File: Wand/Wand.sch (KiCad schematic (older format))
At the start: 20 parts, among them IC1 ATMEGA328P-A, J1 TIP, P1 ISP, P2 BASE, U1 OPA336U, U2 MPU-6050, Y1 16MHz

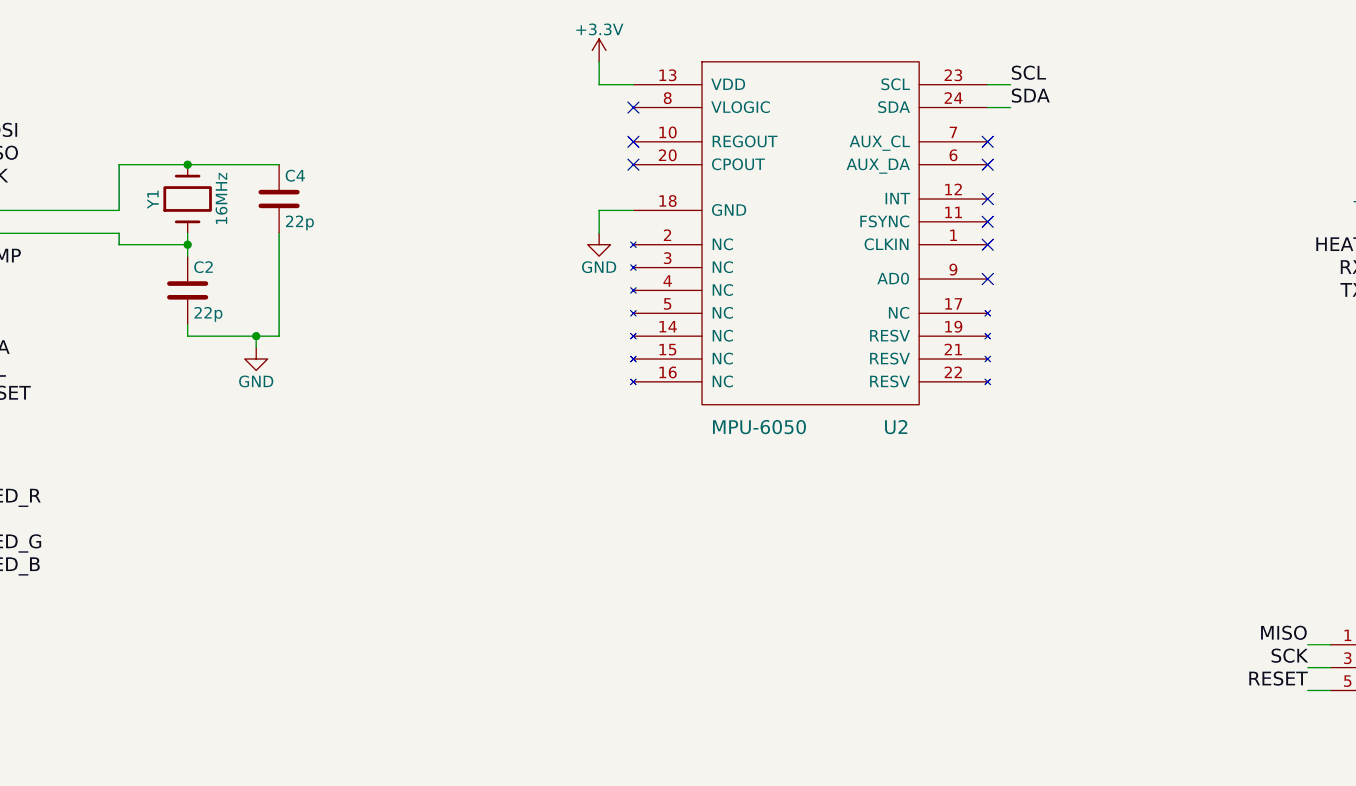
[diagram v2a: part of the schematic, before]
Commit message: Added the support passive components for the MPU-6050.
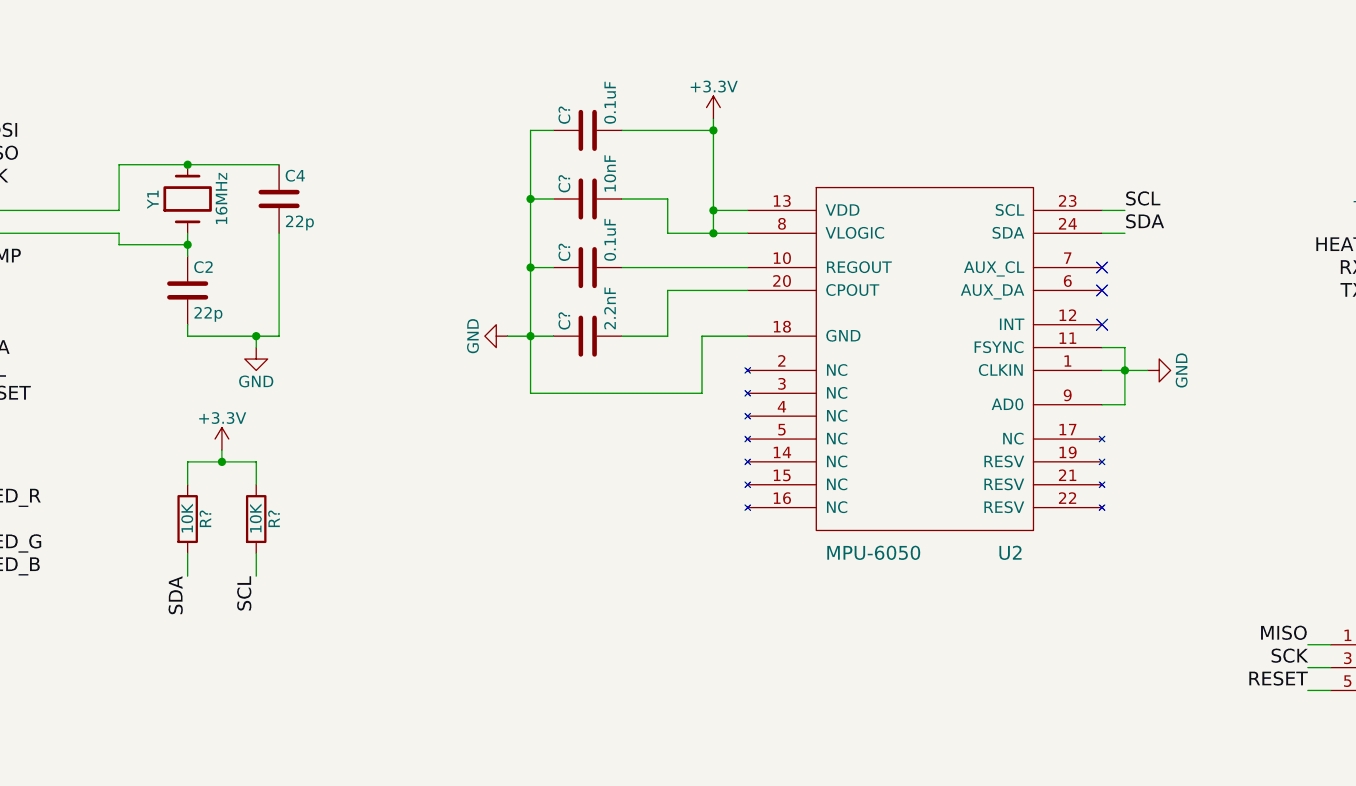
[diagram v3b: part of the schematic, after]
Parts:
- added C?: 2.2nF, symbol C
- added C? (x2): 0.1uF, symbol C
- added C?: 10nF, symbol C
- added R? (x2): 10K, symbol R
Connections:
- net +3V3: now also U2.8 (VLOGIC), C?.2, C?.2, R?.1, R?.1
- net GND: now also U2.1 (CLKIN), U2.11 (FSYNC), U2.9 (AD0), C?.1, C?.1, C?.1, C?.1
- net SCL: now also R?.2
- net SDA: now also R?.2
- net at U2.10 (REGOUT): now also C?.2
- net at U2.20 (CPOUT): now also C?.2
- no-connect marks 23 -> 17
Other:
- moved on the sheet: U2
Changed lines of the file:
@@
 L MPU-6050 U2
 U 1 1 56411594
-P 7450 2100
-F 0 "U2" H 7800 1400 60  0000 C CNN
-F 1 "MPU-6050" H 7200 1400 60  0000 C CNN
-F 2 "" H 7450 1850 60  0000 C CNN
-F 3 "" H 7450 1850 60  0000 C CNN
-	1    7450 2100
+P 7950 2650
+F 0 "U2" H 8300 1950 60  0000 C CNN
+F 1 "MPU-6050" H 7700 1950 60  0000 C CNN
+F 2 "" H 7950 2400 60  0000 C CNN
+F 3 "" H 7950 2400 60  0000 C CNN
+	1    7950 2650
 	1    0    0    -1
 $EndComp
@@
 Wire Wire Line
 	9900 2350 10000 2350
-Text Label 8300 1400 0    60   ~ 0
+Text Label 8800 1950 0    60   ~ 0
 SDA
-Text Label 8300 1300 0    60   ~ 0
+Text Label 8800 1850 0    60   ~ 0
 SCL
 Wire Wire Line
-	8300 1300 8200 1300
-Wire Wire Line
-	8200 1400 8300 1400
-$Comp
-L GND #PWR016
-U 1 1 56419575
-P 6500 1950
-F 0 "#PWR016" H 6500 1700 50  0001 C CNN
-F 1 "GND" H 6500 1800 50  0000 C CNN
-F 2 "" H 6500 1950 60  0000 C CNN
-F 3 "" H 6500 1950 60  0000 C CNN
-	1    6500 1950
-	1    0    0    -1
-$EndComp
-Wire Wire Line
-	6500 1850 6500 1950
-Wire Wire Line
-	6500 1850 6650 1850
-Wire Wire Line
-	6650 1300 6500 1300
-Wire Wire Line
-	6500 1300 6500 1200
+	8800 1850 8700 1850
+Wire Wire Line
+	8700 1950 8800 1950
+Wire Wire Line
+	7000 1850 7150 1850
+Wire Wire Line
+	7000 1450 7000 1950
 Text Label 3750 2500 0    60   ~ 0
 SDA
@@
 NoConn ~ 3600 1350
 NoConn ~ 3600 1250
-NoConn ~ 6650 1400
-NoConn ~ 6650 1550
-NoConn ~ 6650 1650
-NoConn ~ 8200 2150
-NoConn ~ 8200 2000
-NoConn ~ 8200 1900
-NoConn ~ 8200 1800
-NoConn ~ 8200 1650
-NoConn ~ 8200 1550
+NoConn ~ 8700 2350
+NoConn ~ 8700 2200
+NoConn ~ 8700 2100
 $Comp
 L PWR_FLAG #FLG017
@@
 L +3.3V #PWR?
 U 1 1 5647B486
-P 6500 1200
-F 0 "#PWR?" H 6500 1050 50  0001 C CNN
-F 1 "+3.3V" H 6500 1340 50  0000 C CNN
-F 2 "" H 6500 1200 60  0000 C CNN
-F 3 "" H 6500 1200 60  0000 C CNN
-	1    6500 1200
+P 7000 1450
+F 0 "#PWR?" H 7000 1300 50  0001 C CNN
+F 1 "+3.3V" H 7000 1590 50  0000 C CNN
+F 2 "" H 7000 1450 60  0000 C CNN
+F 3 "" H 7000 1450 60  0000 C CNN
+	1    7000 1450
 	1    0    0    -1
 $EndComp
@@
 Text Label 9850 2150 2    60   ~ 0
 RX
+$Comp
+L C C?
+U 1 1 5647F0EB
+P 6450 2400
+F 0 "C?" H 6475 2500 50  0000 L CNN
+F 1 "2.2nF" H 6475 2300 50  0000 L CNN
+F 2 "" H 6488 2250 30  0000 C CNN
+F 3 "" H 6450 2400 60  0000 C CNN
+	1    6450 2400
+	0    -1   -1   0
+$EndComp
+$Comp
+L GND #PWR?
+U 1 1 5647F13E
+P 6100 2400
+F 0 "#PWR?" H 6100 2150 50  0001 C CNN
+F 1 "GND" H 6100 2250 50  0000 C CNN
+F 2 "" H 6100 2400 60  0000 C CNN
+F 3 "" H 6100 2400 60  0000 C CNN
+	1    6100 2400
+	0    1    1    0
+$EndComp
+$Comp
+L GND #PWR?
+U 1 1 5647F1D7
+P 8900 2550
+F 0 "#PWR?" H 8900 2300 50  0001 C CNN
+F 1 "GND" H 8900 2400 50  0000 C CNN
+F 2 "" H 8900 2550 60  0000 C CNN
+F 3 "" H 8900 2550 60  0000 C CNN
+	1    8900 2550
+	0    -1   -1   0
+$EndComp
+Wire Wire Line
+	8800 2700 8700 2700
+$Comp
+L C C?
+U 1 1 5647F6E8
+P 6450 2100
+F 0 "C?" H 6475 2200 50  0000 L CNN
+F 1 "0.1uF" H 6475 2000 50  0000 L CNN
+F 2 "" H 6488 1950 30  0000 C CNN
+F 3 "" H 6450 2100 60  0000 C CNN
+	1    6450 2100
+	0    -1   -1   0
+$EndComp
+Wire Wire Line
+	6800 2200 7150 2200
+Wire Wire Line
+	6600 2400 6800 2400
+Wire Wire Line
+	6600 2100 7150 2100
+Wire Wire Line
+	6300 2100 6200 2100
+Wire Wire Line
+	6200 1500 6200 2650
+Wire Wire Line
+	6100 2400 6300 2400
+Connection ~ 6200 2400
+$Comp
+L C C?
+U 1 1 5647FB65
+P 6450 1800
+F 0 "C?" H 6475 1900 50  0000 L CNN
+F 1 "10nF" H 6475 1700 50  0000 L CNN
+F 2 "" H 6488 1650 30  0000 C CNN
+F 3 "" H 6450 1800 60  0000 C CNN
+	1    6450 1800
+	0    -1   -1   0
+$EndComp
+Wire Wire Line
+	6300 1800 6200 1800
+Connection ~ 6200 2100
+Wire Wire Line
+	7150 1950 6800 1950
+Wire Wire Line
+	6800 1950 6800 1800
+Wire Wire Line
+	6800 1800 6600 1800
+Wire Wire Line
+	6800 2400 6800 2200
+Wire Wire Line
+	7150 2400 6950 2400
+Wire Wire Line
+	6950 2400 6950 2650
+Wire Wire Line
+	6950 2650 6200 2650
+$Comp
+L C C?
+U 1 1 5647FEFB
+P 6450 1500
+F 0 "C?" H 6475 1600 50  0000 L CNN
+F 1 "0.1uF" H 6475 1400 50  0000 L CNN
+F 2 "" H 6488 1350 30  0000 C CNN
+F 3 "" H 6450 1500 60  0000 C CNN
+	1    6450 1500
+	0    -1   -1   0
+$EndComp
+Wire Wire Line
+	6600 1500 7000 1500
+Connection ~ 7000 1500
+Wire Wire Line
+	6300 1500 6200 1500
+Connection ~ 6200 1800
+Connection ~ 7000 1950
+Connection ~ 7000 1850
+Wire Wire Line
+	8700 2450 8800 2450
+Wire Wire Line
+	8800 2450 8800 2700
+Wire Wire Line
+	8700 2550 8900 2550
+Connection ~ 8800 2550
+$Comp
+L R R?
+U 1 1 56481F9A
+P 4700 3200
+F 0 "R?" V 4780 3200 50  0000 C CNN
+F 1 "10K" V 4700 3200 50  0000 C CNN
+F 2 "" V 4630 3200 30  0000 C CNN
+F 3 "" H 4700 3200 30  0000 C CNN
+	1    4700 3200
+	1    0    0    -1
+$EndComp
+$Comp
+L R R?
+U 1 1 56481FFA
+P 5000 3200
+F 0 "R?" V 5080 3200 50  0000 C CNN
+F 1 "10K" V 5000 3200 50  0000 C CNN
+F 2 "" V 4930 3200 30  0000 C CNN
+F 3 "" H 5000 3200 30  0000 C CNN
+	1    5000 3200
+	1    0    0    -1
+$EndComp
+$Comp
+L +3.3V #PWR?
+U 1 1 56482043
+P 4850 2900
+F 0 "#PWR?" H 4850 2750 50  0001 C CNN
+F 1 "+3.3V" H 4850 3040 50  0000 C CNN
+F 2 "" H 4850 2900 60  0000 C CNN
+F 3 "" H 4850 2900 60  0000 C CNN
+	1    4850 2900
+	1    0    0    -1
+$EndComp
+Wire Wire Line
+	4700 3050 4700 2950
+Wire Wire Line
+	4700 2950 5000 2950
+Wire Wire Line
+	4850 2950 4850 2900
+Wire Wire Line
+	5000 2950 5000 3050
+Connection ~ 4850 2950
+Text Label 4700 3450 3    60   ~ 0
+SDA
+Text Label 5000 3450 3    60   ~ 0
+SCL
+Wire Wire Line
+	5000 3350 5000 3450
+Wire Wire Line
+	4700 3350 4700 3450
 $EndSCHEMATC

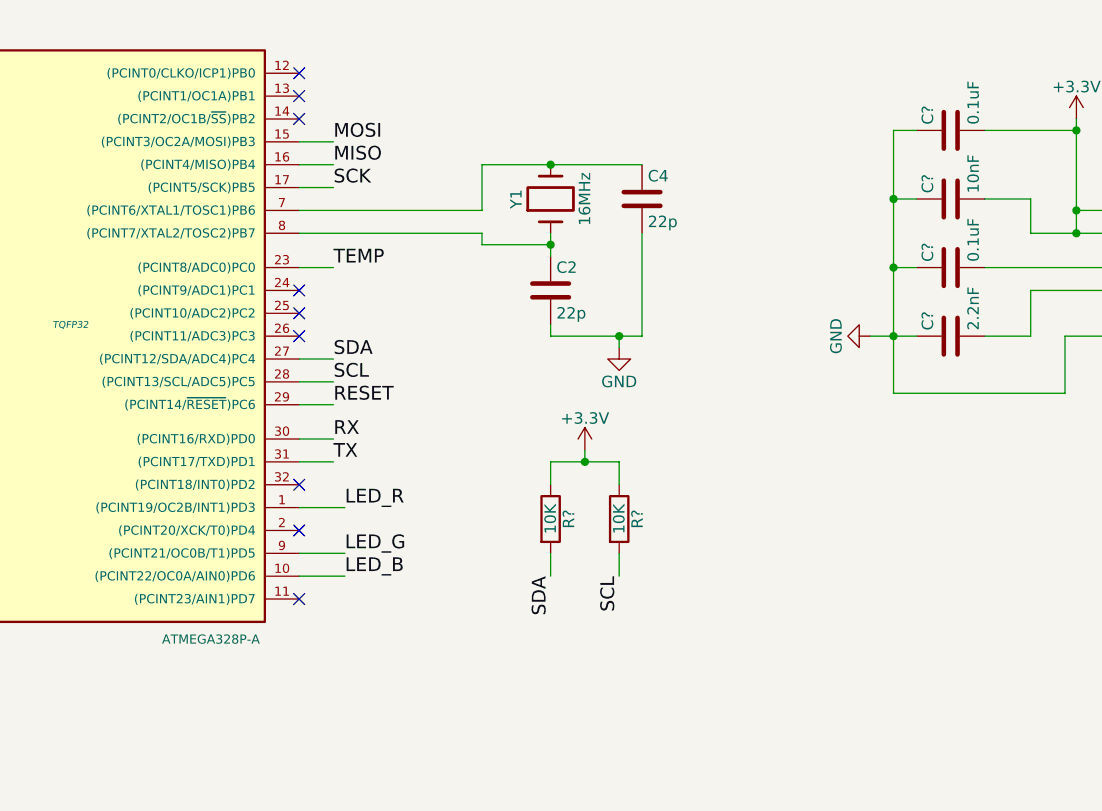
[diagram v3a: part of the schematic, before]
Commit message: Corrected the ATMega 328 part number, needed the 28-pin VQFN package 4x4mm
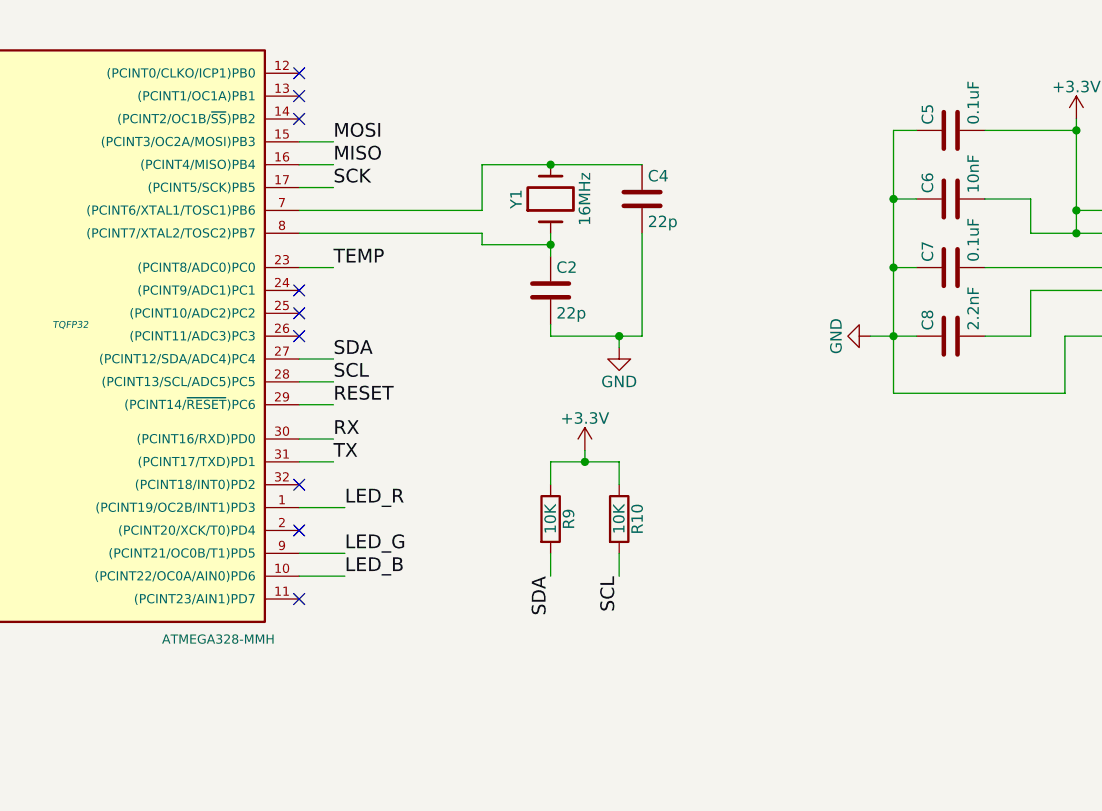
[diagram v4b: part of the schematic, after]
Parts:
- IC1: value ATMEGA328P-A -> ATMEGA328-MMH
- gave numbers to parts that had none: 6
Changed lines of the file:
@@
 P 2600 2350
 F 0 "IC1" H 1850 3600 40  0000 L BNN
-F 1 "ATMEGA328P-A" H 3000 950 40  0000 L BNN
+F 1 "ATMEGA328-MMH" H 3000 950 40  0000 L BNN
 F 2 "TQFP32" H 2600 2350 30  0000 C CIN
 F 3 "" H 2600 2350 60  0000 C CNN
@@
 $EndComp
 $Comp
-L GND #PWR02
+L GND #PWR6
 U 1 1 5641252D
 P 3700 6450
-F 0 "#PWR02" H 3700 6200 50  0001 C CNN
+F 0 "#PWR6" H 3700 6200 50  0001 C CNN
 F 1 "GND" H 3700 6300 50  0000 C CNN
 F 2 "" H 3700 6450 60  0000 C CNN
@@
 SENS
 $Comp
-L GND #PWR03
+L GND #PWR4
 U 1 1 56412884
 P 2650 6450
-F 0 "#PWR03" H 2650 6200 50  0001 C CNN
+F 0 "#PWR4" H 2650 6200 50  0001 C CNN
 F 1 "GND" H 2650 6300 50  0000 C CNN
 F 2 "" H 2650 6450 60  0000 C CNN
@@
 $EndComp
 $Comp
-L GND #PWR04
+L GND #PWR7
 U 1 1 564128BC
 P 4750 6450
-F 0 "#PWR04" H 4750 6200 50  0001 C CNN
+F 0 "#PWR7" H 4750 6200 50  0001 C CNN
 F 1 "GND" H 4750 6300 50  0000 C CNN
 F 2 "" H 4750 6450 60  0000 C CNN
@@
 TEMP
 $Comp
-L +5V #PWR05
+L +5V #PWR3
 U 1 1 564142EE
 P 2000 5050
-F 0 "#PWR05" H 2000 4900 50  0001 C CNN
+F 0 "#PWR3" H 2000 4900 50  0001 C CNN
 F 1 "+5V" H 2000 5190 50  0000 C CNN
 F 2 "" H 2000 5050 60  0000 C CNN
@@
 $EndComp
 $Comp
-L GND #PWR06
+L GND #PWR12
 U 1 1 5641471A
 P 7800 5050
-F 0 "#PWR06" H 7800 4800 50  0001 C CNN
+F 0 "#PWR12" H 7800 4800 50  0001 C CNN
 F 1 "GND" H 7800 4900 50  0000 C CNN
 F 2 "" H 7800 5050 60  0000 C CNN
@@
 TEMP
 $Comp
-L GND #PWR07
+L GND #PWR9
 U 1 1 56415081
 P 5000 2450
-F 0 "#PWR07" H 5000 2200 50  0001 C CNN
+F 0 "#PWR9" H 5000 2200 50  0001 C CNN
 F 1 "GND" H 5000 2300 50  0000 C CNN
 F 2 "" H 5000 2450 60  0000 C CNN
@@
 $EndComp
 $Comp
-L GND #PWR09
+L GND #PWR2
 U 1 1 56415406
 P 1550 3700
-F 0 "#PWR09" H 1550 3450 50  0001 C CNN
+F 0 "#PWR2" H 1550 3450 50  0001 C CNN
 F 1 "GND" H 1550 3550 50  0000 C CNN
 F 2 "" H 1550 3700 60  0000 C CNN
@@
 $EndComp
 $Comp
-L GND #PWR010
+L GND #PWR14
 U 1 1 56416557
 P 9400 5750
-F 0 "#PWR010" H 9400 5500 50  0001 C CNN
+F 0 "#PWR14" H 9400 5500 50  0001 C CNN
 F 1 "GND" H 9400 5600 50  0000 C CNN
 F 2 "" H 9400 5750 60  0000 C CNN
@@
 MOSI
 $Comp
-L GND #PWR012
+L GND #PWR18
 U 1 1 56417D51
 P 10300 4000
-F 0 "#PWR012" H 10300 3750 50  0001 C CNN
+F 0 "#PWR18" H 10300 3750 50  0001 C CNN
 F 1 "GND" H 10300 3850 50  0000 C CNN
 F 2 "" H 10300 4000 60  0000 C CNN
@@
 $EndComp
 $Comp
-L GND #PWR013
+L GND #PWR16
 U 1 1 56417FF2
 P 9900 2350
-F 0 "#PWR013" H 9900 2100 50  0001 C CNN
+F 0 "#PWR16" H 9900 2100 50  0001 C CNN
 F 1 "GND" H 9900 2200 50  0000 C CNN
 F 2 "" H 9900 2350 60  0000 C CNN
@@
 NoConn ~ 8700 2100
 $Comp
-L PWR_FLAG #FLG017
+L PWR_FLAG #FLG1
 U 1 1 5641AE63
 P 10000 1750
-F 0 "#FLG017" H 10000 1845 50  0001 C CNN
+F 0 "#FLG1" H 10000 1845 50  0001 C CNN
 F 1 "PWR_FLAG" H 10000 1930 50  0000 C CNN
 F 2 "" H 10000 1750 60  0000 C CNN
@@
 $EndComp
 $Comp
-L PWR_FLAG #FLG018
+L PWR_FLAG #FLG2
 U 1 1 5641AE9F
 P 10000 2550
-F 0 "#FLG018" H 10000 2645 50  0001 C CNN
+F 0 "#FLG2" H 10000 2645 50  0001 C CNN
 F 1 "PWR_FLAG" H 10000 2730 50  0000 C CNN
 F 2 "" H 10000 2550 60  0000 C CNN
@@
 	10300 3950 10300 4000
 $Comp
-L +3.3V #PWR?
+L +3.3V #PWR15
 U 1 1 5647AD9A
 P 9900 1950
-F 0 "#PWR?" H 9900 1800 50  0001 C CNN
+F 0 "#PWR15" H 9900 1800 50  0001 C CNN
 F 1 "+3.3V" H 9900 2090 50  0000 C CNN
 F 2 "" H 9900 1950 60  0000 C CNN
@@
 $EndComp
 $Comp
-L +3.3V #PWR?
+L +3.3V #PWR11
 U 1 1 5647B486
 P 7000 1450
-F 0 "#PWR?" H 7000 1300 50  0001 C CNN
+F 0 "#PWR11" H 7000 1300 50  0001 C CNN
 F 1 "+3.3V" H 7000 1590 50  0000 C CNN
 F 2 "" H 7000 1450 60  0000 C CNN
@@
 $EndComp
 $Comp
-L +3.3V #PWR?
+L +3.3V #PWR1
 U 1 1 5647BAD5
 P 1450 1200
-F 0 "#PWR?" H 1450 1050 50  0001 C CNN
+F 0 "#PWR1" H 1450 1050 50  0001 C CNN
 F 1 "+3.3V" H 1450 1340 50  0000 C CNN
 F 2 "" H 1450 1200 60  0000 C CNN
@@
 $EndComp
 $Comp
-L +3.3V #PWR?
+L +3.3V #PWR5
 U 1 1 5647C7BA
 P 3700 5050
-F 0 "#PWR?" H 3700 4900 50  0001 C CNN
+F 0 "#PWR5" H 3700 4900 50  0001 C CNN
 F 1 "+3.3V" H 3700 5190 50  0000 C CNN
 F 2 "" H 3700 5050 60  0000 C CNN
@@
 $EndComp
 $Comp
-L +3.3V #PWR?
+L +3.3V #PWR17
 U 1 1 5647DBFE
 P 10300 3700
-F 0 "#PWR?" H 10300 3550 50  0001 C CNN
+F 0 "#PWR17" H 10300 3550 50  0001 C CNN
 F 1 "+3.3V" H 10300 3840 50  0000 C CNN
 F 2 "" H 10300 3700 60  0000 C CNN
@@
 RX
 $Comp
-L C C?
+L C C8
 U 1 1 5647F0EB
 P 6450 2400
-F 0 "C?" H 6475 2500 50  0000 L CNN
+F 0 "C8" H 6475 2500 50  0000 L CNN
 F 1 "2.2nF" H 6475 2300 50  0000 L CNN
 F 2 "" H 6488 2250 30  0000 C CNN
@@
 $EndComp
 $Comp
-L GND #PWR?
+L GND #PWR10
 U 1 1 5647F13E
 P 6100 2400
-F 0 "#PWR?" H 6100 2150 50  0001 C CNN
+F 0 "#PWR10" H 6100 2150 50  0001 C CNN
 F 1 "GND" H 6100 2250 50  0000 C CNN
 F 2 "" H 6100 2400 60  0000 C CNN
@@
 $EndComp
 $Comp
-L GND #PWR?
+L GND #PWR13
 U 1 1 5647F1D7
 P 8900 2550
-F 0 "#PWR?" H 8900 2300 50  0001 C CNN
+F 0 "#PWR13" H 8900 2300 50  0001 C CNN
 F 1 "GND" H 8900 2400 50  0000 C CNN
 F 2 "" H 8900 2550 60  0000 C CNN
@@
 	8800 2700 8700 2700
 $Comp
-L C C?
+L C C7
 U 1 1 5647F6E8
 P 6450 2100
-F 0 "C?" H 6475 2200 50  0000 L CNN
+F 0 "C7" H 6475 2200 50  0000 L CNN
 F 1 "0.1uF" H 6475 2000 50  0000 L CNN
 F 2 "" H 6488 1950 30  0000 C CNN
@@
 Connection ~ 6200 2400
 $Comp
-L C C?
+L C C6
 U 1 1 5647FB65
 P 6450 1800
-F 0 "C?" H 6475 1900 50  0000 L CNN
+F 0 "C6" H 6475 1900 50  0000 L CNN
 F 1 "10nF" H 6475 1700 50  0000 L CNN
 F 2 "" H 6488 1650 30  0000 C CNN
@@
 	6950 2650 6200 2650
 $Comp
-L C C?
+L C C5
 U 1 1 5647FEFB
 P 6450 1500
-F 0 "C?" H 6475 1600 50  0000 L CNN
+F 0 "C5" H 6475 1600 50  0000 L CNN
 F 1 "0.1uF" H 6475 1400 50  0000 L CNN
 F 2 "" H 6488 1350 30  0000 C CNN
@@
 Connection ~ 8800 2550
 $Comp
-L R R?
+L R R9
 U 1 1 56481F9A
 P 4700 3200
-F 0 "R?" V 4780 3200 50  0000 C CNN
+F 0 "R9" V 4780 3200 50  0000 C CNN
 F 1 "10K" V 4700 3200 50  0000 C CNN
 F 2 "" V 4630 3200 30  0000 C CNN
@@
 $EndComp
 $Comp
-L R R?
+L R R10
 U 1 1 56481FFA
 P 5000 3200
-F 0 "R?" V 5080 3200 50  0000 C CNN
+F 0 "R10" V 5080 3200 50  0000 C CNN
 F 1 "10K" V 5000 3200 50  0000 C CNN
 F 2 "" V 4930 3200 30  0000 C CNN
@@
 $EndComp
 $Comp
-L +3.3V #PWR?
+L +3.3V #PWR8
 U 1 1 56482043
 P 4850 2900
-F 0 "#PWR?" H 4850 2750 50  0001 C CNN
+F 0 "#PWR8" H 4850 2750 50  0001 C CNN
 F 1 "+3.3V" H 4850 3040 50  0000 C CNN
 F 2 "" H 4850 2900 60  0000 C CNN
